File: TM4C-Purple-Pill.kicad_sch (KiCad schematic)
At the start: 33 parts, among them IC1 TM4C123GH6PMI7R, J1 Conn_01x22, J2 Conn_01x22, J3 Conn_02x05_Top_Bottom, J4 USB_C_Receptacle_USB2.0_16P, U1 LD1117S33TR_SOT223, Y1 ABM3-16.000MHZ-B2-T, Y2 AB26TRB-32.768KHZ-T

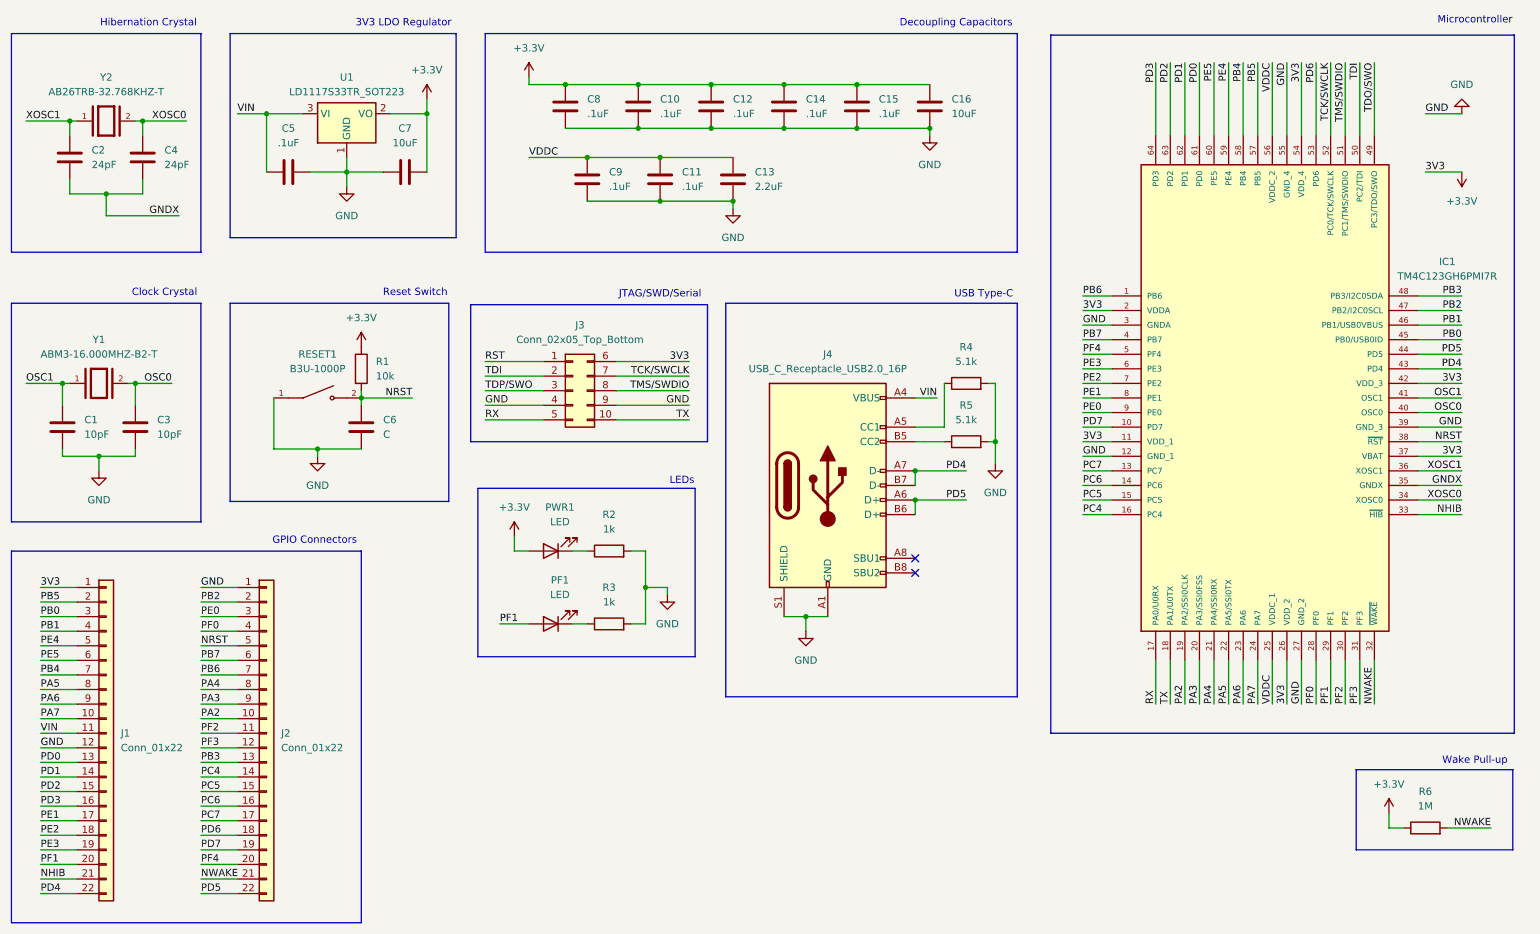
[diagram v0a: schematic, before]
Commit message: Switch Type-C to Micro-B
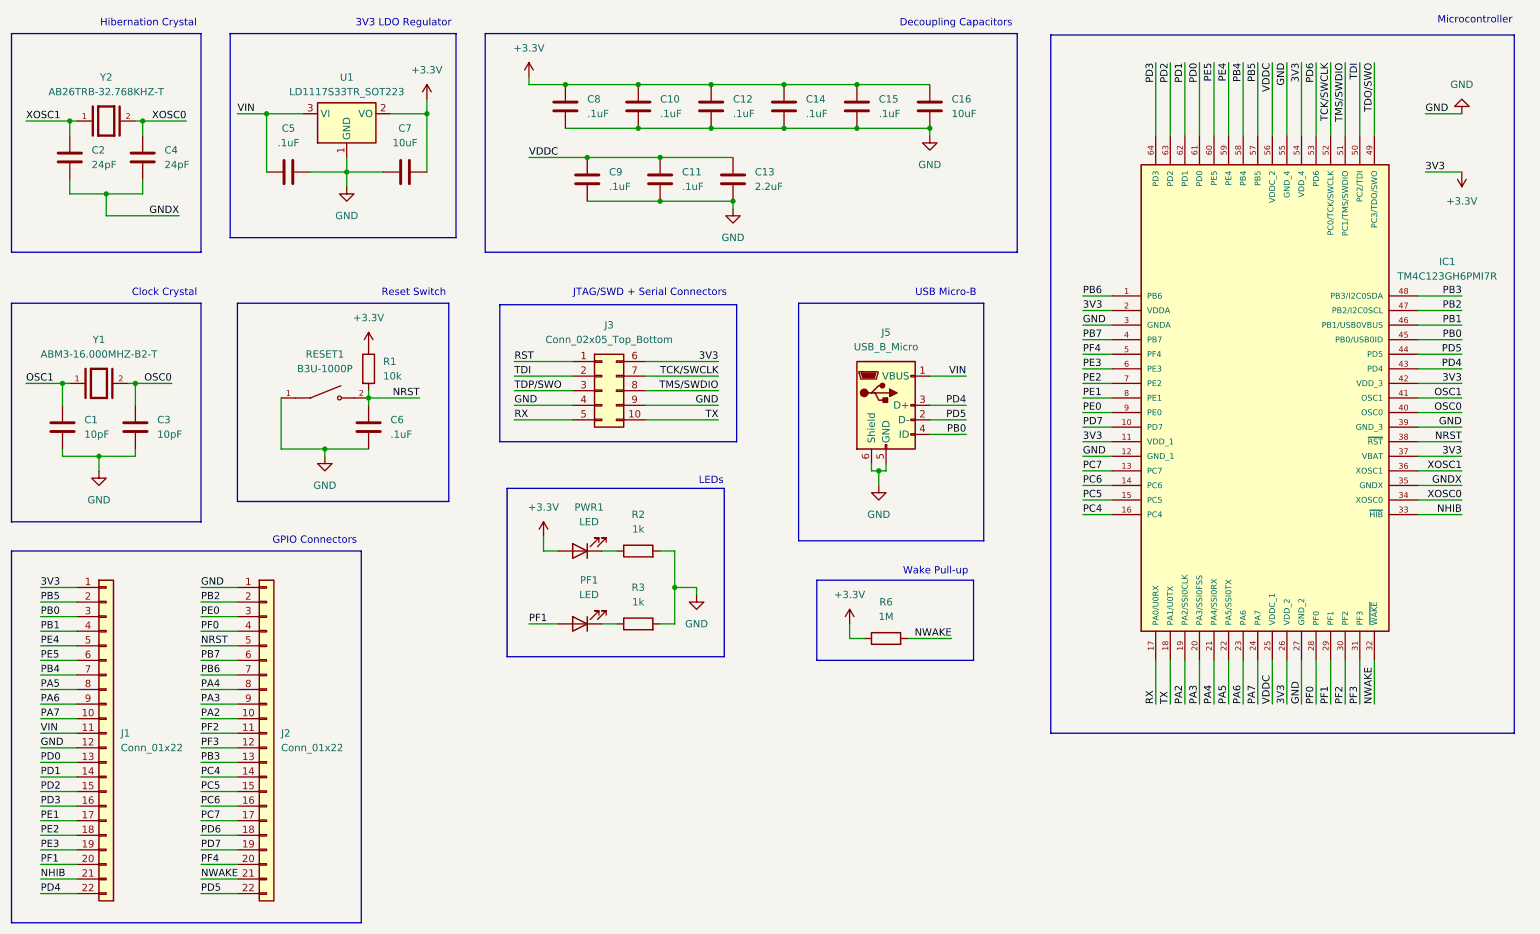
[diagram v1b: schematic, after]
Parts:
- removed J4: USB_C_Receptacle_USB2.0_16P, Connector_USB:USB_C_Receptacle_G-Switch_GT-USB-7010ASV, symbol Connector:USB_C_Receptacle_USB2.0_16P
- removed R4, R5: 5.1k, symbol Device:R
- added J5: USB_B_Micro, symbol Connector:USB_B_Micro
- C6: value C -> .1uF
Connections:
- net GND: now also J5.5 (GND), J5.6 (Shield)
- net PB0: now also J5.4 (ID)
- net PD4: now also J5.3 (D+)
- net PD5: now also J5.2 (D-)
- net VIN: now also J5.1 (VBUS)
- no-connect marks 2 -> 0
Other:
- note added: "JTAG/SWD + Serial Connectors"
- note added: "USB Micro-B"
- note removed: "JTAG/SWD/Serial"
- note removed: "USB Type-C"
- company: Created by Rolando Rosales -> Rolando Rosales
- moved on the sheet: C6, J3, PF1, PWR1, R1, R2, R3, R6, RESET1

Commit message: Mostly finishied pinout. Will redo entire PCB with original GPIO configuration, as it is too messy
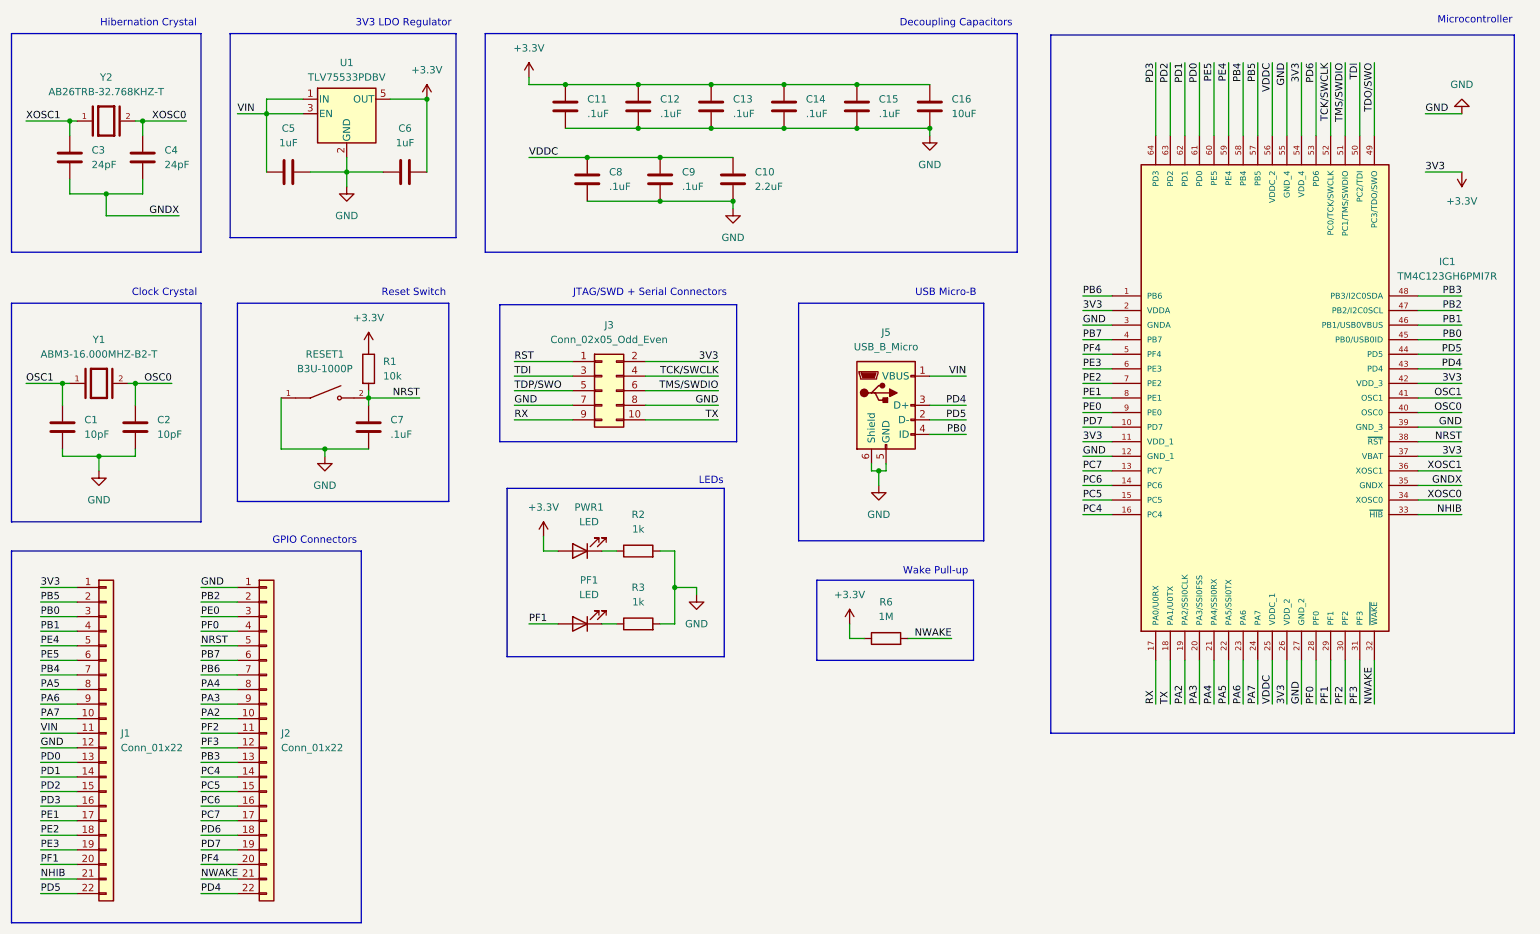
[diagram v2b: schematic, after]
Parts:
- removed J3: Conn_02x05_Top_Bottom, symbol Connector_Generic:Conn_02x05_Top_Bottom
- removed U1: LD1117S33TR_SOT223, Package_TO_SOT_SMD:SOT-223-3_TabPin2, symbol Regulator_Linear:LD1117S33TR_SOT223
- added J3: Conn_02x05_Odd_Even, Connector_PinHeader_2.54mm:PinHeader_2x05_P2.54mm_Horizontal, symbol Connector_Generic:Conn_02x05_Odd_Even
- added U1: TLV75533PDBV, Package_TO_SOT_SMD:SOT-23-5, symbol Regulator_Linear:TLV75533PDBV
- C1, C14, C15, C4: footprint (none) -> Capacitor_SMD:C_0402_1005Metric
- C10: renamed from C13; footprint (none) -> Capacitor_SMD:C_0603_1608Metric
- C11: renamed from C8; footprint (none) -> Capacitor_SMD:C_0402_1005Metric
- C12: renamed from C10; footprint (none) -> Capacitor_SMD:C_0402_1005Metric
- C13: renamed from C12; footprint (none) -> Capacitor_SMD:C_0402_1005Metric
- C16: footprint (none) -> Capacitor_SMD:C_0603_1608Metric
- C2: renamed from C3; footprint (none) -> Capacitor_SMD:C_0402_1005Metric
- C3: renamed from C2; footprint (none) -> Capacitor_SMD:C_0402_1005Metric
- C5: value .1uF -> 1uF; footprint (none) -> Capacitor_SMD:C_0603_1608Metric
- C6: renamed from C7; value 10uF -> 1uF; footprint (none) -> Capacitor_SMD:C_0603_1608Metric
- C7: renamed from C6; footprint (none) -> Capacitor_SMD:C_0402_1005Metric
- C8: renamed from C9; footprint (none) -> Capacitor_SMD:C_0402_1005Metric
- C9: renamed from C11; footprint (none) -> Capacitor_SMD:C_0402_1005Metric
- J1, J2: footprint (none) -> Connector_PinHeader_2.54mm:PinHeader_1x22_P2.54mm_Vertical
- J5: footprint (none) -> Connector_USB:USB_Micro-B_Amphenol_10104110_Horizontal
- PF1, PWR1: footprint (none) -> LED_SMD:LED_1206_3216Metric
- R1, R2, R3, R6: footprint (none) -> Resistor_SMD:R_0402_1005Metric
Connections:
- net +3.3V: now also J3.2 (Pin_2), U1.5 (OUT)
- net GND: now also J3.7 (Pin_7), J3.8 (Pin_8), U1.2 (GND)
- net PD4: now also J2.22 (Pin_22); no longer J1.22 (Pin_22)
- net PD5: now also J1.22 (Pin_22); no longer J2.22 (Pin_22)
- net RST: now also J3.1 (Pin_1)
- net RX: now also J3.9 (Pin_9)
- net TCK/SWCLK: now also J3.4 (Pin_4)
- net TDI: now also J3.3 (Pin_3)
- net TDP/SWO: now also J3.5 (Pin_5)
- net TMS/SWDIO: now also J3.6 (Pin_6)
- net TX: now also J3.10 (Pin_10)
- net VIN: now also U1.1 (IN), U1.3 (EN)

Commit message: Rehauled GPIO pinout. Need to find NRST wiring
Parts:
- removed J5: USB_B_Micro, Connector_USB:USB_Micro-B_Amphenol_10104110_Horizontal, symbol Connector:USB_B_Micro
- added 5.1k1: R5, Resistor_SMD:R_0402_1005Metric, symbol Device:R
- added C17: 1uF, Capacitor_SMD:C_0603_1608Metric, symbol Device:C
- added D1: ESD9B3.3ST5G, Diode_SMD:D_SOD-923, symbol Diode:ESD9B3.3ST5G
- added J4: USB_C_Receptacle_USB2.0_16P, Connector_USB:USB_C_Receptacle_G-Switch_GT-USB-7010ASV, symbol Connector:USB_C_Receptacle_USB2.0_16P
- added R4: 5.1k, Resistor_SMD:R_0402_1005Metric, symbol Device:R
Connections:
- net RST is gone; now on net NRST: J3.1 (Pin_1)
- net TDP/SWO is gone; now on net TDO/SWO: J3.5 (Pin_5)
- net +3.3V: now also J2.1 (Pin_1); no longer J1.1 (Pin_1)
- net GND: now also J2.2 (Pin_2), J2.22 (Pin_22), 5.1k1.1, C17.2, D1.1 (A1), J4.A1 (GND), J4.A12 (GND), J4.B1 (GND), J4.B12 (GND), J4.S1 (SHIELD), R4.2; no longer J1.12 (Pin_12), J2.1 (Pin_1)
- net NHIB: now also J2.10 (Pin_10); no longer J1.21 (Pin_21)
- net NRST: now also J2.9 (Pin_9); no longer J2.5 (Pin_5)
- net NWAKE: now also J2.11 (Pin_11); no longer J2.21 (Pin_21)
- net PA2: now also J2.21 (Pin_21); no longer J2.10 (Pin_10)
- net PA3: now also J2.20 (Pin_20); no longer J2.9 (Pin_9)
- net PA4: now also J2.19 (Pin_19); no longer J2.8 (Pin_8)
- net PA5: now also J2.18 (Pin_18); no longer J1.8 (Pin_8)
- net PA6: now also J2.17 (Pin_17); no longer J1.9 (Pin_9)
- net PA7: now also J2.16 (Pin_16); no longer J1.10 (Pin_10)
- net PB0: now also J2.6 (Pin_6); no longer J1.3 (Pin_3)
- net PB1: now also J2.5 (Pin_5); no longer J1.4 (Pin_4)
- net PB2: now also J2.4 (Pin_4); no longer J2.2 (Pin_2)
- net PB3: now also J2.3 (Pin_3); no longer J2.13 (Pin_13)
- net PB4: now also J1.3 (Pin_3); no longer J1.7 (Pin_7)
- net PB6: now also J1.10 (Pin_10); no longer J2.7 (Pin_7)
- net PB7: now also J1.11 (Pin_11); no longer J2.6 (Pin_6)
- net PC4: now also J1.21 (Pin_21); no longer J2.14 (Pin_14)
- net PC5: now also J1.20 (Pin_20); no longer J2.15 (Pin_15)
- net PC6: now also J1.19 (Pin_19); no longer J2.16 (Pin_16)
- net PC7: now also J1.18 (Pin_18); no longer J2.17 (Pin_17)
- net PD0: now also J1.6 (Pin_6); no longer J1.13 (Pin_13)
- net PD1: now also J1.7 (Pin_7); no longer J1.14 (Pin_14)
- net PD2: now also J1.8 (Pin_8); no longer J1.15 (Pin_15)
- net PD3: now also J1.9 (Pin_9); no longer J1.16 (Pin_16)
- net PD4: now also J2.8 (Pin_8), J4.A6 (D+), J4.B6 (D+); no longer J2.22 (Pin_22)
- net PD5: now also J2.7 (Pin_7), J4.A7 (D-), J4.B7 (D-); no longer J1.22 (Pin_22)
- net PD6: now also J1.1 (Pin_1); no longer J2.18 (Pin_18)
- net PD7: now also J1.17 (Pin_17); no longer J2.19 (Pin_19)
- net PE0: now also J1.16 (Pin_16); no longer J2.3 (Pin_3)
- net PE1: now also J1.15 (Pin_15); no longer J1.17 (Pin_17)
- net PE2: now also J1.14 (Pin_14); no longer J1.18 (Pin_18)
- net PE3: now also J1.13 (Pin_13); no longer J1.19 (Pin_19)
- net PE4: now also J1.4 (Pin_4); no longer J1.5 (Pin_5)
- net PE5: now also J1.5 (Pin_5); no longer J1.6 (Pin_6)
- net PF0: now also J2.15 (Pin_15); no longer J2.4 (Pin_4)
- net PF1: now also J2.14 (Pin_14); no longer J1.20 (Pin_20)
- net PF2: now also J2.13 (Pin_13); no longer J2.11 (Pin_11)
- net PF4: now also J1.12 (Pin_12); no longer J2.20 (Pin_20)
- net VIN renamed VBUS
- net VBUS: now also J1.22 (Pin_22), C17.1, D1.2 (A2), J4.A4 (VBUS), J4.A9 (VBUS), J4.B4 (VBUS), J4.B9 (VBUS); no longer J1.11 (Pin_11)
- new net: J4.A5 (CC1), R4.1
- new net: 5.1k1.2, J4.B5 (CC2)
- no-connect marks 0 -> 2
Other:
- note added: "NWAKE Pull-up"
- note added: "Power/User LEDs"
- note added: "USB Type-C"
- note removed: "LEDs"
- note removed: "USB Micro-B"
- note removed: "Wake Pull-up"
- moved on the sheet: PF1, PWR1, R2, R3, R6

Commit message: Revision 0.3 with ground plane
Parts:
- removed C17: 1uF, Capacitor_SMD:C_0603_1608Metric, symbol Device:C
- removed D1: ESD9B3.3ST5G, Diode_SMD:D_SOD-923, symbol Diode:ESD9B3.3ST5G
- removed Y2: AB26TRB-32.768KHZ-T, AB26TRB-32.768KHZ-T:XTAL_AB26TRB-32.768KHZ-T, symbol AB26TRB-32.768KHZ-T:AB26TRB-32.768KHZ-T
- added U2: USBLC6-2SC6, Package_TO_SOT_SMD:SOT-23-6, symbol Power_Protection:USBLC6-2SC6
- added Y2: ABS07-32.768KHZ-T, ABS07-32.768KHZ-T:XTAL_ABS07-32.768KHZ-T, symbol ABS07-32.768KHZ-T:ABS07-32.768KHZ-T
- R5: renamed from 5.1k1; value R5 -> 5.1k
- renumbered RESET1 to RST1
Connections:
- net GND: now also U2.2 (GND)
- net PD4: now also U2.4 (I/O2); no longer J4.A6 (D+), J4.B6 (D+)
- net PD5: now also U2.6 (I/O1); no longer J4.A7 (D-), J4.B7 (D-)
- net VBUS: now also U2.5 (VBUS)
- net XOSC0: now also Y2.2
- net XOSC1: now also Y2.1
- new net: J4.A7 (D-), J4.B7 (D-), U2.1 (I/O1)
- new net: J4.A6 (D+), J4.B6 (D+), U2.3 (I/O2)
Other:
- moved on the sheet: PF1, PWR1, R2, R3, R6
